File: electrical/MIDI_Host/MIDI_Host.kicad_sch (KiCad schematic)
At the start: 54 parts, among them CN1 USB-CON-AF-LCP-Offset, J1 MC-107DM, J2 (NF), SW1 TC-1109DE-C-G, SW2 ST-0-102-C03-N003-RS, U1 ESP32-S3-WROOM-1U, U2 BL1551B, U3 BL1551B, U4 BL1551B, U5 BL1551B, U6 SESRV05-4, U7 SESRV05-4, U8 74HC165

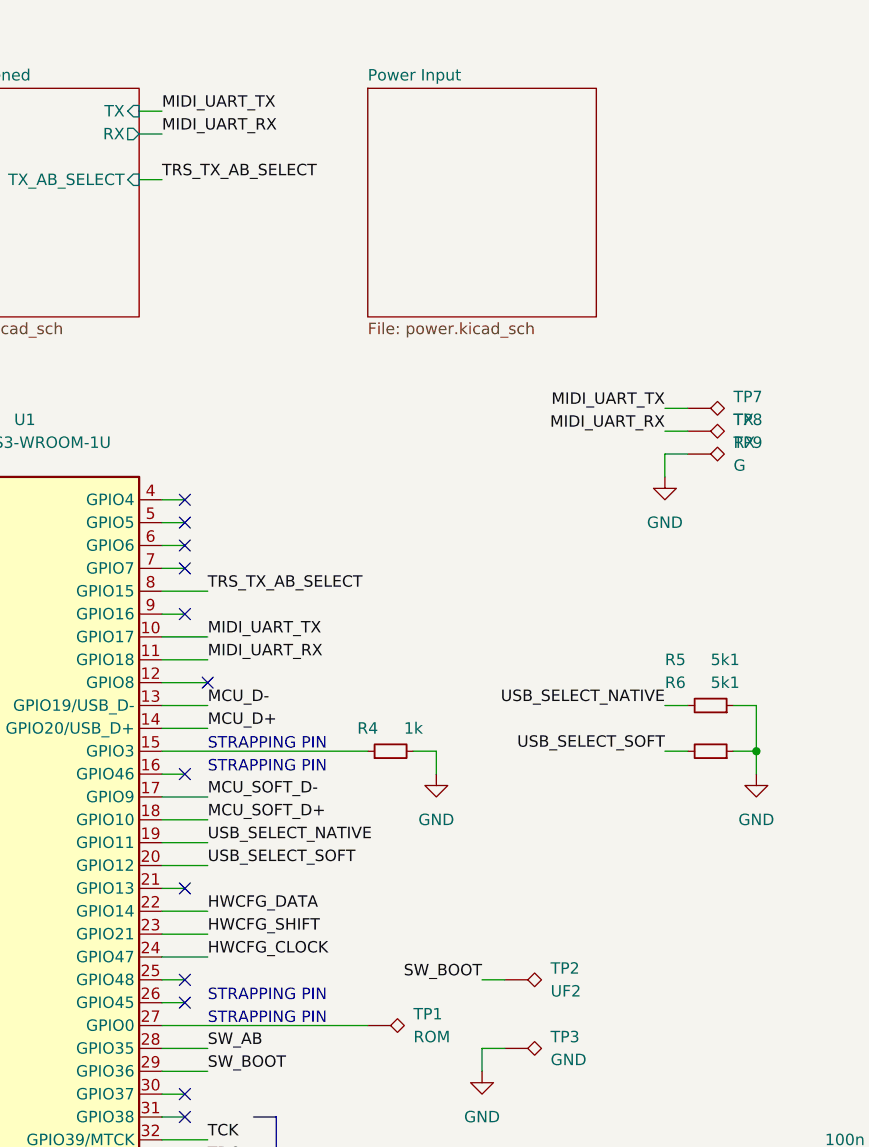
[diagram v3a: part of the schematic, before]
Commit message: SUKU PMIC enable pin signal added
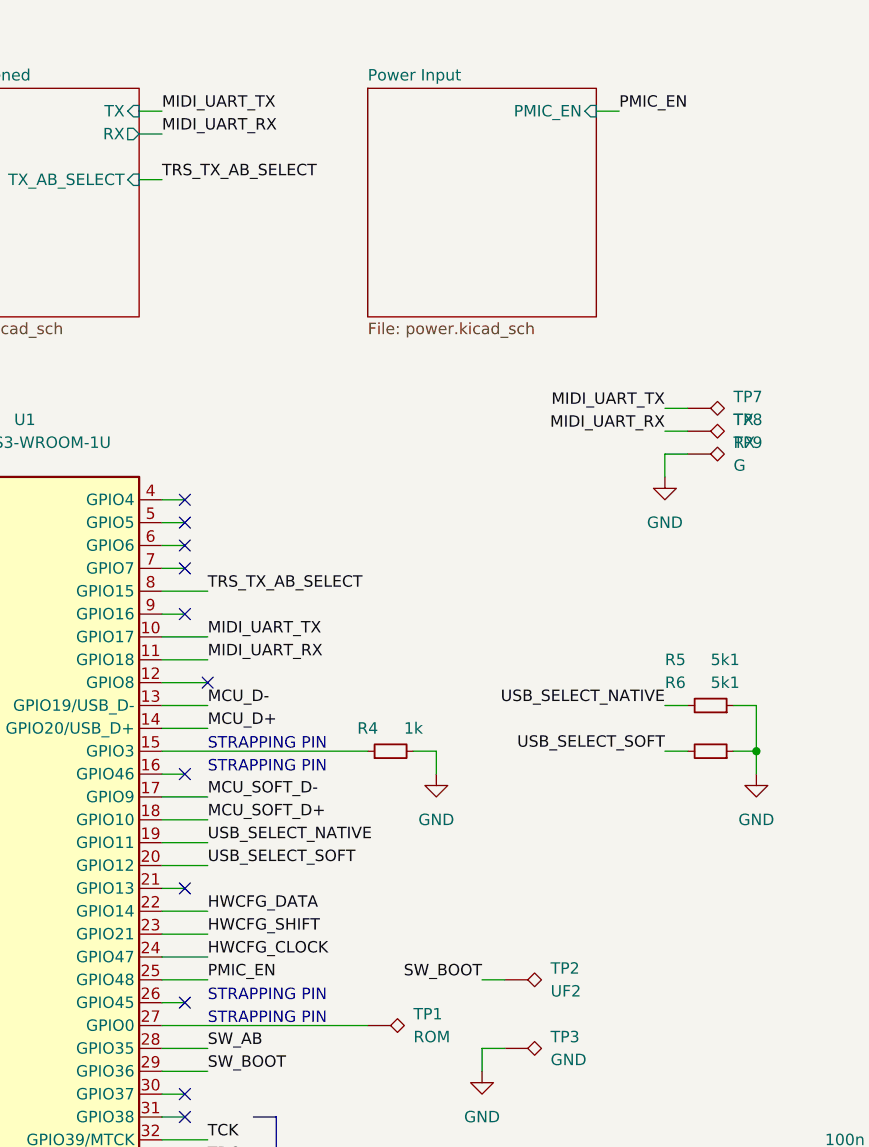
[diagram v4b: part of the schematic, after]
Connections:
- net PMIC_EN: now reaches U1.25 (GPIO48)
- no-connect marks 23 -> 22
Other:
- sheet Power Input ports: added PMIC_EN; removed none
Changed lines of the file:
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@@
   (no_connect (at 60.96 111.76))
   (no_connect (at 60.96 124.46))
-  (no_connect (at 60.96 121.92))
   (no_connect (at 60.96 134.62))
   (no_connect (at 60.96 137.16))
@@
     (stroke (width 0) (type default) (color 0 0 0 0))
   )
+  (wire (pts (xy 106.68 25.4) (xy 109.22 25.4))
+    (stroke (width 0) (type default) (color 0 0 0 0))
+  )
   (wire (pts (xy 58.42 137.16) (xy 60.96 137.16))
     (stroke (width 0) (type default) (color 0 0 0 0))
@@
     (stroke (width 0) (type default) (color 0 0 0 0))
   )
-  (wire (pts (xy 58.42 121.92) (xy 60.96 121.92))
-    (stroke (width 0) (type default) (color 0 0 0 0))
-  )
   (wire (pts (xy 175.26 147.32) (xy 175.26 144.78))
     (stroke (width 0) (type default) (color 0 0 0 0))
@@
     (stroke (width 0) (type default) (color 0 0 0 0))
   )
+  (wire (pts (xy 58.42 121.92) (xy 63.5 121.92))
+    (stroke (width 0) (type default) (color 0 0 0 0))
+  )
   (wire (pts (xy 170.18 177.8) (xy 175.26 177.8))
     (stroke (width 0) (type default) (color 0 0 0 0))
@@
     (effects (font (size 1.27 1.27)) (justify left bottom))
   )
+  (label "PMIC_EN" (at 109.22 25.4 0)
+    (effects (font (size 1.27 1.27)) (justify left bottom))
+  )
   (label "MCU_D-" (at 43.18 248.92 180)
     (effects (font (size 1.27 1.27)) (justify right bottom))
@@
     (effects (font (size 1.27 1.27)) (justify left bottom))
   )
+  (label "PMIC_EN" (at 63.5 121.92 0)
+    (effects (font (size 1.27 1.27)) (justify left bottom))
+  )
   (label "CONN_C_D+" (at 195.58 99.06 90)
     (effects (font (size 1.27 1.27)) (justify left bottom))
@@
       (effects (font (size 1.27 1.27)) (justify left top))
     )
+    (pin "PMIC_EN" input (at 106.68 25.4 0)
+      (effects (font (size 1.27 1.27)) (justify right))
+    )
   )
   (sheet (at 30.48 22.86) (size 25.4 25.4) (fields_autoplaced)
@@
       (reference "#PWR093") (unit 1) (value "GND") (footprint "")
     )
-    (path "/60c177f6-9f45-413f-893d-8d98077afbe8/1aa98b62-440d-4aa3-a0f9-2199bc6577ff"
-      (reference "#PWR094") (unit 1) (value "GND") (footprint "")
-    )
     (path "/60c177f6-9f45-413f-893d-8d98077afbe8/e3d8f794-479e-4a01-b9f8-3489c6d220a8"
-      (reference "#PWR095") (unit 1) (value "+5V") (footprint "")
+      (reference "#PWR094") (unit 1) (value "+5V") (footprint "")
+    )
+    (path "/60c177f6-9f45-413f-893d-8d98077afbe8/1aa98b62-440d-4aa3-a0f9-2199bc6577ff"
+      (reference "#PWR095") (unit 1) (value "GND") (footprint "")
     )
     (path "/60c177f6-9f45-413f-893d-8d98077afbe8/f2726f5f-c915-474d-af1f-69fe1055a580"
       (reference "#PWR096") (unit 1) (value "GND") (footprint "")
     )
+    (path "/60c177f6-9f45-413f-893d-8d98077afbe8/42df331b-66a0-4f70-9b3a-16bdd036e8c3"
+      (reference "#PWR097") (unit 1) (value "+3V3") (footprint "")
+    )
     (path "/60c177f6-9f45-413f-893d-8d98077afbe8/90802568-6815-441f-8637-c7a2d92ade42"
-      (reference "#PWR097") (unit 1) (value "GND") (footprint "")
+      (reference "#PWR098") (unit 1) (value "GND") (footprint "")
+    )
+    (path "/60c177f6-9f45-413f-893d-8d98077afbe8/fd25d4fb-5058-4a93-8bda-cb84cd249e63"
+      (reference "#PWR099") (unit 1) (value "GND") (footprint "")
     )
     (path "/60c177f6-9f45-413f-893d-8d98077afbe8/7a4a4c79-22db-4784-b9f0-b54e7908cdb0"
-      (reference "#PWR098") (unit 1) (value "+5V") (footprint "")
+      (reference "#PWR0100") (unit 1) (value "+5V") (footprint "")
     )
     (path "/60c177f6-9f45-413f-893d-8d98077afbe8/5f5f3ff7-73b5-47db-b45c-2304d1ee66c2"
-      (reference "#PWR099") (unit 1) (value "GND") (footprint "")
+      (reference "#PWR0101") (unit 1) (value "GND") (footprint "")
     )
     (path "/60c177f6-9f45-413f-893d-8d98077afbe8/c4b0a315-6f2c-4109-a79e-1c748bddd65c"
-      (reference "#PWR0100") (unit 1) (value "GND") (footprint "")
+      (reference "#PWR0102") (unit 1) (value "GND") (footprint "")
     )
     (path "/60c177f6-9f45-413f-893d-8d98077afbe8/c99a7925-3334-4a72-940d-fc06c39a419a"
-      (reference "#PWR0101") (unit 1) (value "GND") (footprint "")
+      (reference "#PWR0103") (unit 1) (value "GND") (footprint "")
     )
     (path "/60c177f6-9f45-413f-893d-8d98077afbe8/132e00fb-0ccd-498f-9b6c-fd6e93de93d1"
-      (reference "#PWR0102") (unit 1) (value "GND") (footprint "")
+      (reference "#PWR0104") (unit 1) (value "GND") (footprint "")
     )
     (path "/60c177f6-9f45-413f-893d-8d98077afbe8/e9b69af2-67db-47a9-961a-d1bb94df3fa1"
-      (reference "#PWR0103") (unit 1) (value "GND") (footprint "")
+      (reference "#PWR0105") (unit 1) (value "GND") (footprint "")
     )
     (path "/60c177f6-9f45-413f-893d-8d98077afbe8/cc741e4a-caf8-4fa0-a1eb-7a452183c306"
-      (reference "#PWR0104") (unit 1) (value "GND") (footprint "")
+      (reference "#PWR0106") (unit 1) (value "GND") (footprint "")
     )
     (path "/60c177f6-9f45-413f-893d-8d98077afbe8/76c92079-7964-45a1-b273-f99c9809103e"
-      (reference "#PWR0105") (unit 1) (value "GND") (footprint "")
+      (reference "#PWR0107") (unit 1) (value "GND") (footprint "")
     )
     (path "/60c177f6-9f45-413f-893d-8d98077afbe8/d018c7e8-6967-4f4f-8592-675755362525"
-      (reference "#PWR0106") (unit 1) (value "GND") (footprint "")
+      (reference "#PWR0108") (unit 1) (value "GND") (footprint "")
     )
     (path "/60c177f6-9f45-413f-893d-8d98077afbe8/891d0dce-2ff6-4b3f-a4ad-2a6a7e3617df"
-      (reference "#PWR0107") (unit 1) (value "+3V3") (footprint "")
+      (reference "#PWR0109") (unit 1) (value "+3V3") (footprint "")
     )
     (path "/60c177f6-9f45-413f-893d-8d98077afbe8/323e75b4-a147-4171-998a-4ad6f77a232a"
-      (reference "#PWR0108") (unit 1) (value "GND") (footprint "")
+      (reference "#PWR0110") (unit 1) (value "GND") (footprint "")
     )
     (path "/60c177f6-9f45-413f-893d-8d98077afbe8/747dff1f-5103-4bb4-8475-586975bf5995"
-      (reference "#PWR0109") (unit 1) (value "+5V") (footprint "")
+      (reference "#PWR0111") (unit 1) (value "+5V") (footprint "")
     )
     (path "/60c177f6-9f45-413f-893d-8d98077afbe8/7bac28dc-f982-4303-a1c3-f743c244e412"
-      (reference "#PWR0110") (unit 1) (value "GND") (footprint "")
+      (reference "#PWR0112") (unit 1) (value "GND") (footprint "")
     )
     (path "/60c177f6-9f45-413f-893d-8d98077afbe8/22cb5fdc-9c06-432f-a602-6efd41dd96fa"
-      (reference "#PWR0111") (unit 1) (value "VBUS") (footprint "")
+      (reference "#PWR0113") (unit 1) (value "VBUS") (footprint "")
     )
     (path "/60c177f6-9f45-413f-893d-8d98077afbe8/5bed8a93-bb1f-4bd8-be03-378c12eb4bbb"
-      (reference "#PWR0112") (unit 1) (value "VBUS") (footprint "")
+      (reference "#PWR0114") (unit 1) (value "VBUS") (footprint "")
     )
     (path "/60c177f6-9f45-413f-893d-8d98077afbe8/423e41ef-b74d-4065-ad4d-ca6c302b626c"
-      (reference "#PWR0113") (unit 1) (value "GND") (footprint "")
+      (reference "#PWR0115") (unit 1) (value "GND") (footprint "")
     )
     (path "/78083a21-ffc6-4dac-bfdb-cbc4d5f4490c/26c9c776-25f0-450d-9602-87a8f4632b1a"
@@
       (reference "C18") (unit 1) (value "56u") (footprint "Capacitor_SMD:CP_Elec_5x5.8")
     )
-    (path "/60c177f6-9f45-413f-893d-8d98077afbe8/b1be133b-6109-457f-973f-3e36bfe9a06e"
-      (reference "C19") (unit 1) (value "10n") (footprint "suku_basics:CAP_0402")
-    )
     (path "/60c177f6-9f45-413f-893d-8d98077afbe8/d03477a4-3d9e-48b7-a3f3-2e34a7ddd91d"
-      (reference "C20") (unit 1) (value "10u") (footprint "suku_basics:CAP_0402")
+      (reference "C19") (unit 1) (value "10u") (footprint "suku_basics:CAP_0402")
+    )
+    (path "/60c177f6-9f45-413f-893d-8d98077afbe8/b1be133b-6109-457f-973f-3e36bfe9a06e"
+      (reference "C20") (unit 1) (value "10n") (footprint "suku_basics:CAP_0402")
     )
     (path "/60c177f6-9f45-413f-893d-8d98077afbe8/d77b48be-1983-4c38-86ae-eb4926bd3aa4"
@@
       (reference "R17") (unit 1) (value "5k1") (footprint "suku_basics:RES_0402")
     )
+    (path "/60c177f6-9f45-413f-893d-8d98077afbe8/dbb7d2e4-7f3f-43d7-905b-a6786572065a"
+      (reference "R18") (unit 1) (value "10k (NF)") (footprint "suku_basics:RES_0402")
+    )
+    (path "/60c177f6-9f45-413f-893d-8d98077afbe8/1d44d517-0624-4fae-b063-0309062577e5"
+      (reference "R19") (unit 1) (value "10k") (footprint "suku_basics:RES_0402")
+    )
     (path "/60c177f6-9f45-413f-893d-8d98077afbe8/2d6f8c53-c2ae-4f2d-88e8-351c4cb83401"
-      (reference "R18") (unit 1) (value "10k") (footprint "suku_basics:RES_0402")
+      (reference "R20") (unit 1) (value "10k") (footprint "suku_basics:RES_0402")
     )
     (path "/60c177f6-9f45-413f-893d-8d98077afbe8/3aac17af-0e9c-4905-88f1-c41a8ddc82a9"
-      (reference "R19") (unit 1) (value "3k24") (footprint "suku_basics:RES_0402")
+      (reference "R21") (unit 1) (value "3k24") (footprint "suku_basics:RES_0402")
     )
     (path "/60c177f6-9f45-413f-893d-8d98077afbe8/bdeda33e-a503-4613-83e1-5e0b082b8fd9"
-      (reference "R20") (unit 1) (value "3k4") (footprint "suku_basics:RES_0402")
+      (reference "R22") (unit 1) (value "3k4") (footprint "suku_basics:RES_0402")
     )
     (path "/be6da077-d179-463a-af26-1bac671e85bf"

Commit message: SUKU bootloader updated
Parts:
- added C1: 1u, suku_basics:CAP_0402, symbol suku_basics:CAP
- added R2: 5k1, suku_basics:RES_0402, symbol suku_basics:RES
- added SW1, SW2: C2905169, Button_Switch_SMD:SW_SPST_CK_RS282G05A3, symbol Switch:SW_SPST
- renumbered C9 to C10, C10 to C11, C11 to C12, C1 to C2, C2 to C3, C3 to C4, C4 to C5, C5 to C6, C6 to C7, C7 to C8, C8 to C9, R9 to R10, R10 to R11, R11 to R12, R2 to R3, R3 to R4, R4 to R5, R5 to R6, R6 to R7, R7 to R8, R8 to R9, SW1 to SW3, SW2 to SW4, TP4 to TP1, TP5 to TP2, TP6 to TP3, TP7 to TP4, TP8 to TP5, TP9 to TP6, TP2 to TP7, TP1 to TP8, TP3 to TP9
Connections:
- net GND: now also C1.2, SW1.1 (A), SW2.1 (A)
- net ESP_BOOT0: now reaches TP8.1, U1.27 (GPIO0)
- net ESP_BOOT0: now also SW2.2 (B)
- net at R1.2: now also R2.1; no longer U1.3 (EN)
- new net ESP_RESET: C1.1, R2.2, SW1.2 (B), U1.3 (EN)
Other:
- moved on the sheet: TP7, TP8, TP9

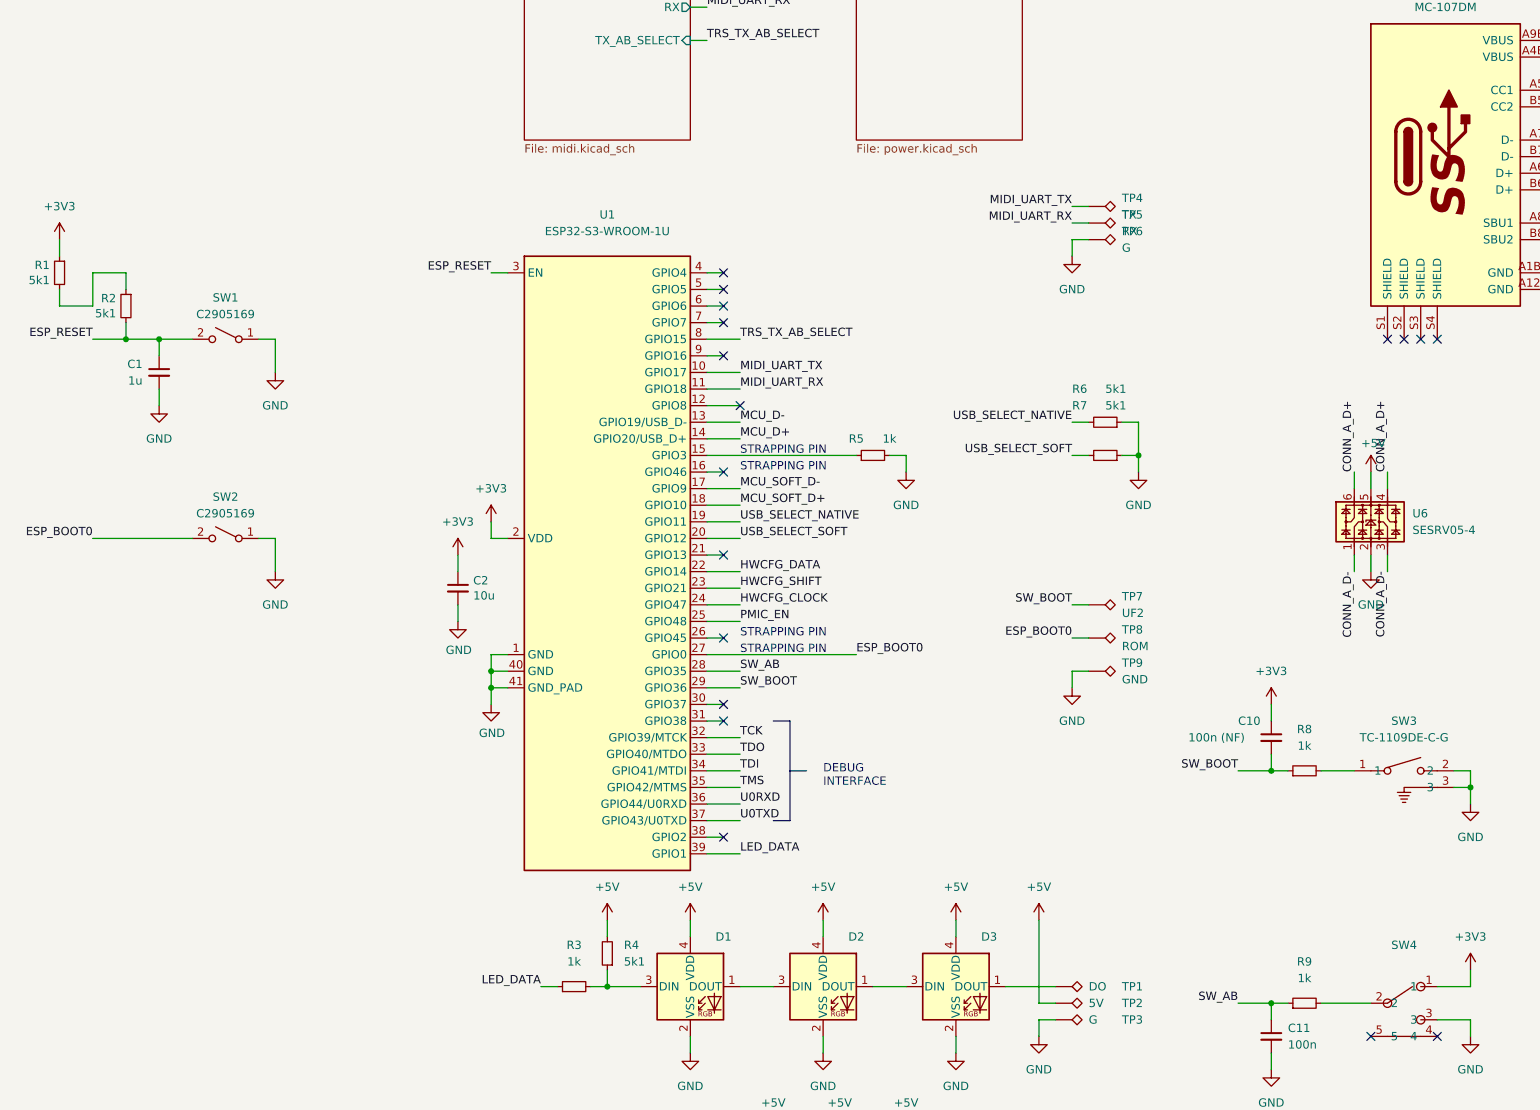
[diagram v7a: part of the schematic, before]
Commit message: SUKU updated layout done, cicd updated with position offset and v7 runner
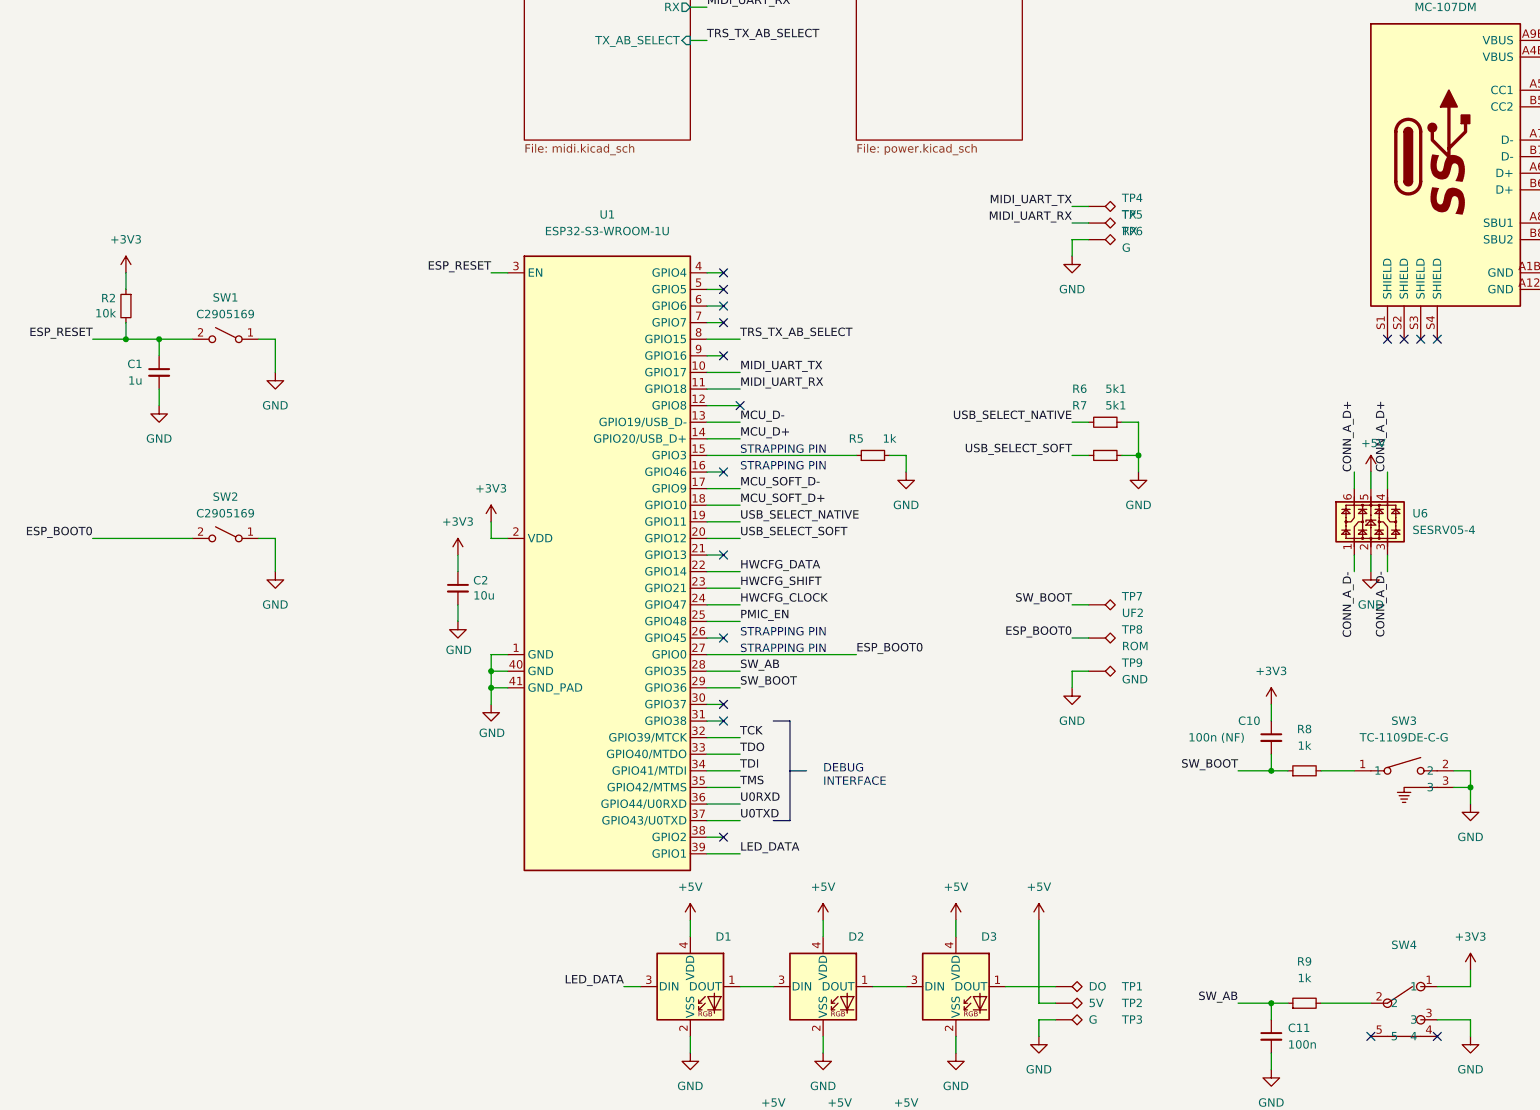
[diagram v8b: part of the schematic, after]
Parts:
- removed R1, R4: 5k1, suku_basics:RES_0402, symbol suku_basics:RES
- removed R3: 1k, suku_basics:RES_0402, symbol suku_basics:RES
- R2: value 5k1 -> 10k
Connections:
- net +3V3: now also R2.1
- net LED_DATA: now also D1.3 (DIN)
